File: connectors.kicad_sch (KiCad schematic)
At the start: 4 parts, among them J1 Conn_01x04_Pin, J2 Conn_01x04_Pin, J3 Conn_01x09_Pin, J4 Conn_02x03_Odd_Even

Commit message: completed symbol to footprint assocciations
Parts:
- J1, J2: footprint (none) -> Connector_PinHeader_2.54mm:PinHeader_1x04_P2.54mm_Vertical
- J3: footprint (none) -> Connector_PinHeader_2.54mm:PinHeader_1x09_P2.54mm_Vertical
- J4: footprint (none) -> Connector_PinHeader_2.54mm:PinHeader_2x03_P2.54mm_Vertical
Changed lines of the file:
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@@
       (effects (font (size 1.27 1.27)))
     )
-    (property "Footprint" "" (at 80.9856 38.4921 0)
+    (property "Footprint" "Connector_PinHeader_2.54mm:PinHeader_1x04_P2.54mm_Vertical" (at 80.9856 38.4921 0)
       (effects (font (size 1.27 1.27)) hide)
     )
@@
       (effects (font (size 1.27 1.27)))
     )
-    (property "Footprint" "" (at 51.1813 73.9876 0)
+    (property "Footprint" "Connector_PinHeader_2.54mm:PinHeader_1x09_P2.54mm_Vertical" (at 51.1813 73.9876 0)
       (effects (font (size 1.27 1.27)) hide)
     )
@@
       (effects (font (size 1.27 1.27)))
     )
-    (property "Footprint" "" (at 84.6425 70.754 0)
+    (property "Footprint" "Connector_PinHeader_2.54mm:PinHeader_2x03_P2.54mm_Vertical" (at 84.6425 70.754 0)
       (effects (font (size 1.27 1.27)) hide)
     )
@@
       (effects (font (size 1.27 1.27)))
     )
-    (property "Footprint" "" (at 51.0801 39.4084 0)
+    (property "Footprint" "Connector_PinHeader_2.54mm:PinHeader_1x04_P2.54mm_Vertical" (at 51.0801 39.4084 0)
       (effects (font (size 1.27 1.27)) hide)
     )

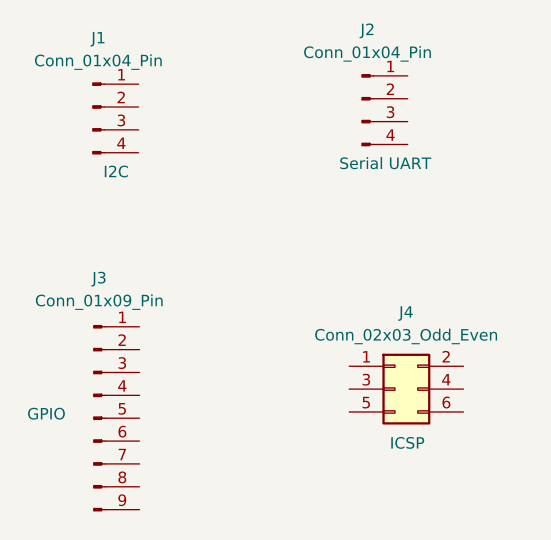
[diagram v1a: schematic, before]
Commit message: Completed wiring in schematic
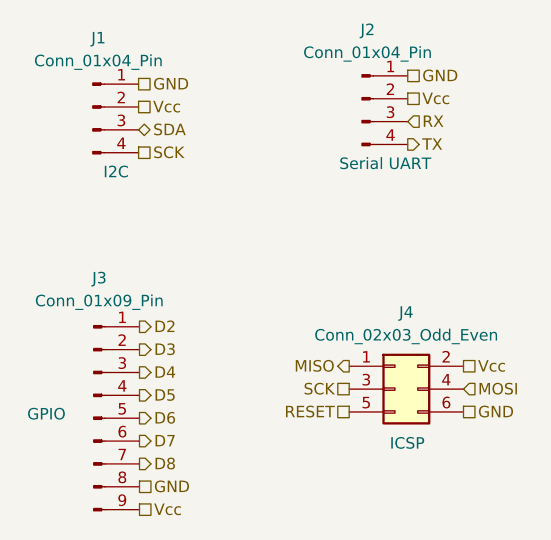
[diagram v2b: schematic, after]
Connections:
- net GND: now reaches J2.1 (Pin_1)
- net GND: now also J1.1 (Pin_1), J3.8 (Pin_8), J4.6 (Pin_6)
- net Vcc: now reaches J2.2 (Pin_2)
- net Vcc: now also J1.2 (Pin_2), J3.9 (Pin_9), J4.2 (Pin_2)
- net RX: now reaches J2.3 (Pin_3)
- net TX: now reaches J2.4 (Pin_4)
- net D2: now reaches J3.1 (Pin_1)
- net D3: now reaches J3.2 (Pin_2)
- net D4: now reaches J3.3 (Pin_3)
- net D5: now reaches J3.4 (Pin_4)
- net D6: now reaches J3.5 (Pin_5)
- net D7: now reaches J3.6 (Pin_6)
- net D8: now reaches J3.7 (Pin_7)
- net MISO: now reaches J4.1 (Pin_1)
- net SCK: now reaches J4.3 (Pin_3)
- net SCK: now also J1.4 (Pin_4)
- net MOSI: now reaches J4.4 (Pin_4)
- net RESET: now reaches J4.5 (Pin_5)
- net SDA: now reaches J1.3 (Pin_3)
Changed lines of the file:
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@@
 (kicad_sch (version 20230121) (generator eeschema)
   (paper "A4")
+  (hierarchical_label "MISO" (shape output) (at 79.5625 68.214 180) (fields_autoplaced)
+    (effects (font (size 1.27 1.27)) (justify right))
+  )
+  (hierarchical_label "SCK" (shape passive) (at 56.1601 44.4884 0) (fields_autoplaced)
+    (effects (font (size 1.27 1.27)) (justify left))
+  )
+  (hierarchical_label "GND" (shape passive) (at 56.1601 36.8684 0) (fields_autoplaced)
+    (effects (font (size 1.27 1.27)) (justify left))
+  )
+  (hierarchical_label "SDA" (shape bidirectional) (at 56.1601 41.9484 0) (fields_autoplaced)
+    (effects (font (size 1.27 1.27)) (justify left))
+  )
+  (hierarchical_label "D5" (shape output) (at 56.2613 71.4476 0) (fields_autoplaced)
+    (effects (font (size 1.27 1.27)) (justify left))
+  )
+  (hierarchical_label "TX" (shape output) (at 86.0656 43.5721 0) (fields_autoplaced)
+    (effects (font (size 1.27 1.27)) (justify left))
+  )
+  (hierarchical_label "Vcc" (shape passive) (at 92.2625 68.214 0) (fields_autoplaced)
+    (effects (font (size 1.27 1.27)) (justify left))
+  )
+  (hierarchical_label "D7" (shape output) (at 56.2613 76.5276 0) (fields_autoplaced)
+    (effects (font (size 1.27 1.27)) (justify left))
+  )
+  (hierarchical_label "MOSI" (shape input) (at 92.2625 70.754 0) (fields_autoplaced)
+    (effects (font (size 1.27 1.27)) (justify left))
+  )
+  (hierarchical_label "RESET" (shape passive) (at 79.5625 73.294 180) (fields_autoplaced)
+    (effects (font (size 1.27 1.27)) (justify right))
+  )
+  (hierarchical_label "SCK" (shape passive) (at 79.5625 70.754 180) (fields_autoplaced)
+    (effects (font (size 1.27 1.27)) (justify right))
+  )
+  (hierarchical_label "D4" (shape output) (at 56.2613 68.9076 0) (fields_autoplaced)
+    (effects (font (size 1.27 1.27)) (justify left))
+  )
+  (hierarchical_label "Vcc" (shape passive) (at 56.2613 84.1476 0) (fields_autoplaced)
+    (effects (font (size 1.27 1.27)) (justify left))
+  )
+  (hierarchical_label "Vcc" (shape passive) (at 86.0656 38.4921 0) (fields_autoplaced)
+    (effects (font (size 1.27 1.27)) (justify left))
+  )
+  (hierarchical_label "D8" (shape output) (at 56.2613 79.0676 0) (fields_autoplaced)
+    (effects (font (size 1.27 1.27)) (justify left))
+  )
+  (hierarchical_label "D2" (shape output) (at 56.2613 63.8276 0) (fields_autoplaced)
+    (effects (font (size 1.27 1.27)) (justify left))
+  )
+  (hierarchical_label "Vcc" (shape passive) (at 56.1601 39.4084 0) (fields_autoplaced)
+    (effects (font (size 1.27 1.27)) (justify left))
+  )
+  (hierarchical_label "D3" (shape output) (at 56.2613 66.3676 0) (fields_autoplaced)
+    (effects (font (size 1.27 1.27)) (justify left))
+  )
+  (hierarchical_label "GND" (shape passive) (at 92.2625 73.294 0) (fields_autoplaced)
+    (effects (font (size 1.27 1.27)) (justify left))
+  )
+  (hierarchical_label "GND" (shape passive) (at 86.0656 35.9521 0) (fields_autoplaced)
+    (effects (font (size 1.27 1.27)) (justify left))
+  )
+  (hierarchical_label "RX" (shape input) (at 86.0656 41.0321 0) (fields_autoplaced)
+    (effects (font (size 1.27 1.27)) (justify left))
+  )
+  (hierarchical_label "GND" (shape passive) (at 56.2613 81.6076 0) (fields_autoplaced)
+    (effects (font (size 1.27 1.27)) (justify left))
+  )
+  (hierarchical_label "D6" (shape output) (at 56.2613 73.9876 0) (fields_autoplaced)
+    (effects (font (size 1.27 1.27)) (justify left))
+  )
   (symbol (lib_id "Connector:Conn_01x04_Pin") (at 80.9856 38.4921 0) (unit 1)
     (in_bom yes) (on_board yes) (dnp no)

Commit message: Fixed two defects in the schematic
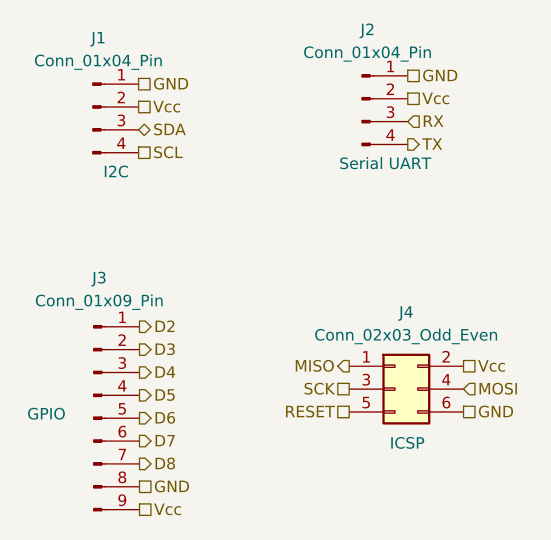
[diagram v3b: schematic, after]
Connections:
- net SCK: no longer J1.4 (Pin_4)
- new net SCL: J1.4 (Pin_4)
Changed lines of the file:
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@@
     (effects (font (size 1.27 1.27)) (justify right))
   )
-  (hierarchical_label "SCK" (shape passive) (at 56.1601 44.4884 0) (fields_autoplaced)
+  (hierarchical_label "SCL" (shape passive) (at 56.1601 44.4884 0) (fields_autoplaced)
     (effects (font (size 1.27 1.27)) (justify left))
   )
